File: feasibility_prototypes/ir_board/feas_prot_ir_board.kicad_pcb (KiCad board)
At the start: 2 copper layers, 1.3 x 7 mm, 10 parts, among them P1 CONN_01X03, P2 CONN_01X03, P3 CONN_02X08, P4 CONN_02X08, Q1 APT2012P3BT

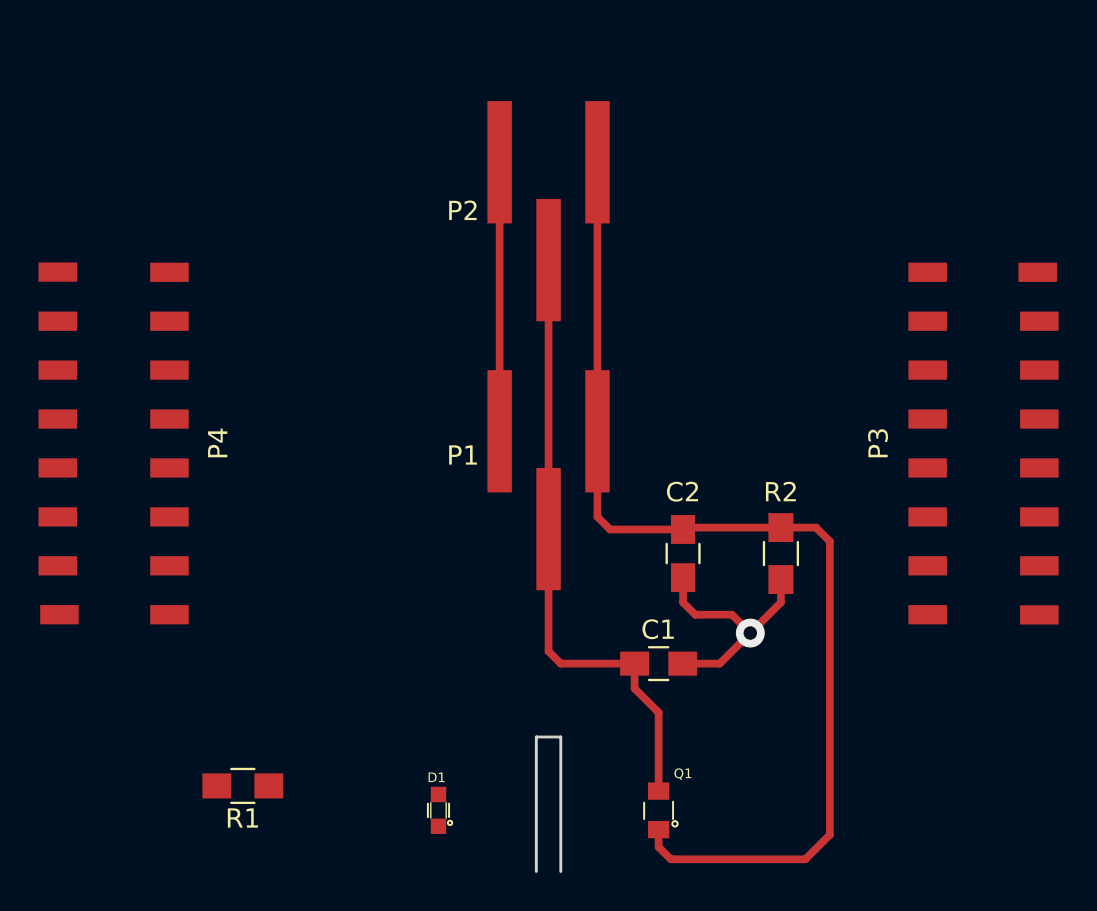
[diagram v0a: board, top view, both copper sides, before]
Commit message: Added RJ11 connector to processor board, finished IR board.
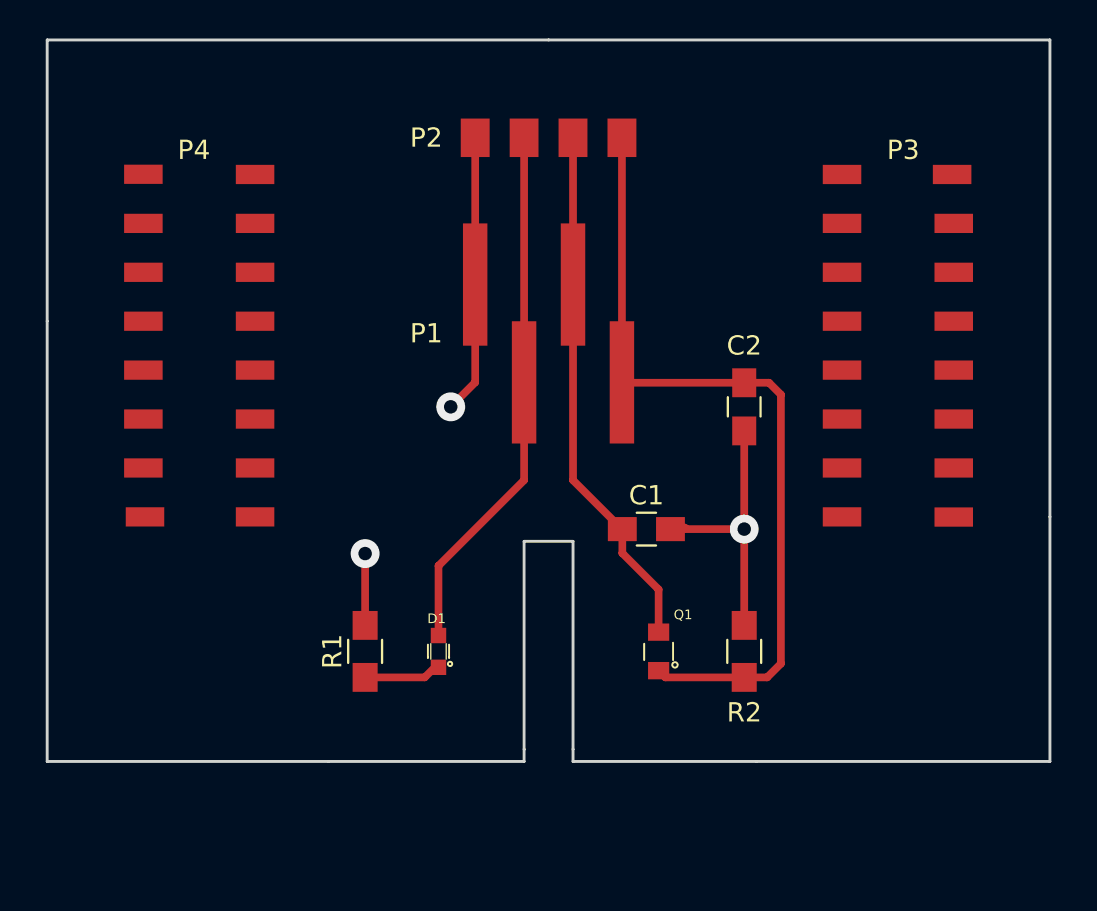
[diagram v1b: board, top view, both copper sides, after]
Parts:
- P1: value CONN_01X03 -> CONN_01X04; footprint med_conn_prototype_footprints:Sullins_SMD_pin_header_1x3_GBC36SABN-M30 -> med_conn_prototype_footprints:Sullins_SMD_pin_header_1x4_GBC36SABN-M30
- P2: value CONN_01X03 -> CONN_01X04; footprint med_conn_prototype_footprints:Sullins_SMD_pin_header_1x3_GBC36SABN-M30 -> med_conn_prototype_footprints:wire_solder_pad_2.54mm_1x4
- moved R1 9.44 mm to (141.0, 102.9), turned to 90 degrees
- moved C2 8.26 mm to (160.7, 90.2)
- moved D1 8.25 mm to (144.8, 102.9)
- moved Q1 8.25 mm to (156.2, 102.9)
- moved P1 7.62 mm to (150.5, 78.7)
- moved C1 7.01 mm to (155.6, 96.5)
- moved P3 6.75 mm to (161.9, 87.0)
- moved P4 6.75 mm to (139.1, 87.0)
- moved R2 5.43 mm to (160.7, 102.9), turned to 90 degrees
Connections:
- P1 pad 1: Net-(D1-Pad2) -> GND
- P1 pad 2: Net-(C1-Pad1) -> Net-(D1-Pad2)
- P1 pad 3: Net-(C2-Pad1) -> Net-(C1-Pad1)
- P2 pad 1: Net-(D1-Pad2) -> GND
- P2 pad 2: Net-(C1-Pad1) -> Net-(D1-Pad2)
- P2 pad 3: Net-(C2-Pad1) -> Net-(C1-Pad1)
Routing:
- net GND: track 13.5 -> 31.7 mm, vias 1 -> 3
- net Net-(C2-Pad1): track 56.9 -> 42.1 mm
- net Net-(D1-Pad2): track 14.0 -> 27.7 mm
- net Net-(C1-Pad1): track 32.2 -> 27.5 mm
- net Net-(D1-Pad1): track 0.00 -> 4.03 mm
- added copper zone on B.Cu, net GND
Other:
- board size 1.3 x 7 mm -> 52.1 x 37.5 mm
